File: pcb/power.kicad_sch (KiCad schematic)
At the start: 42 parts, among them Q1 AO3400A, U1 SIC431AED-T1-GE3, U2 TPS564247DRLR

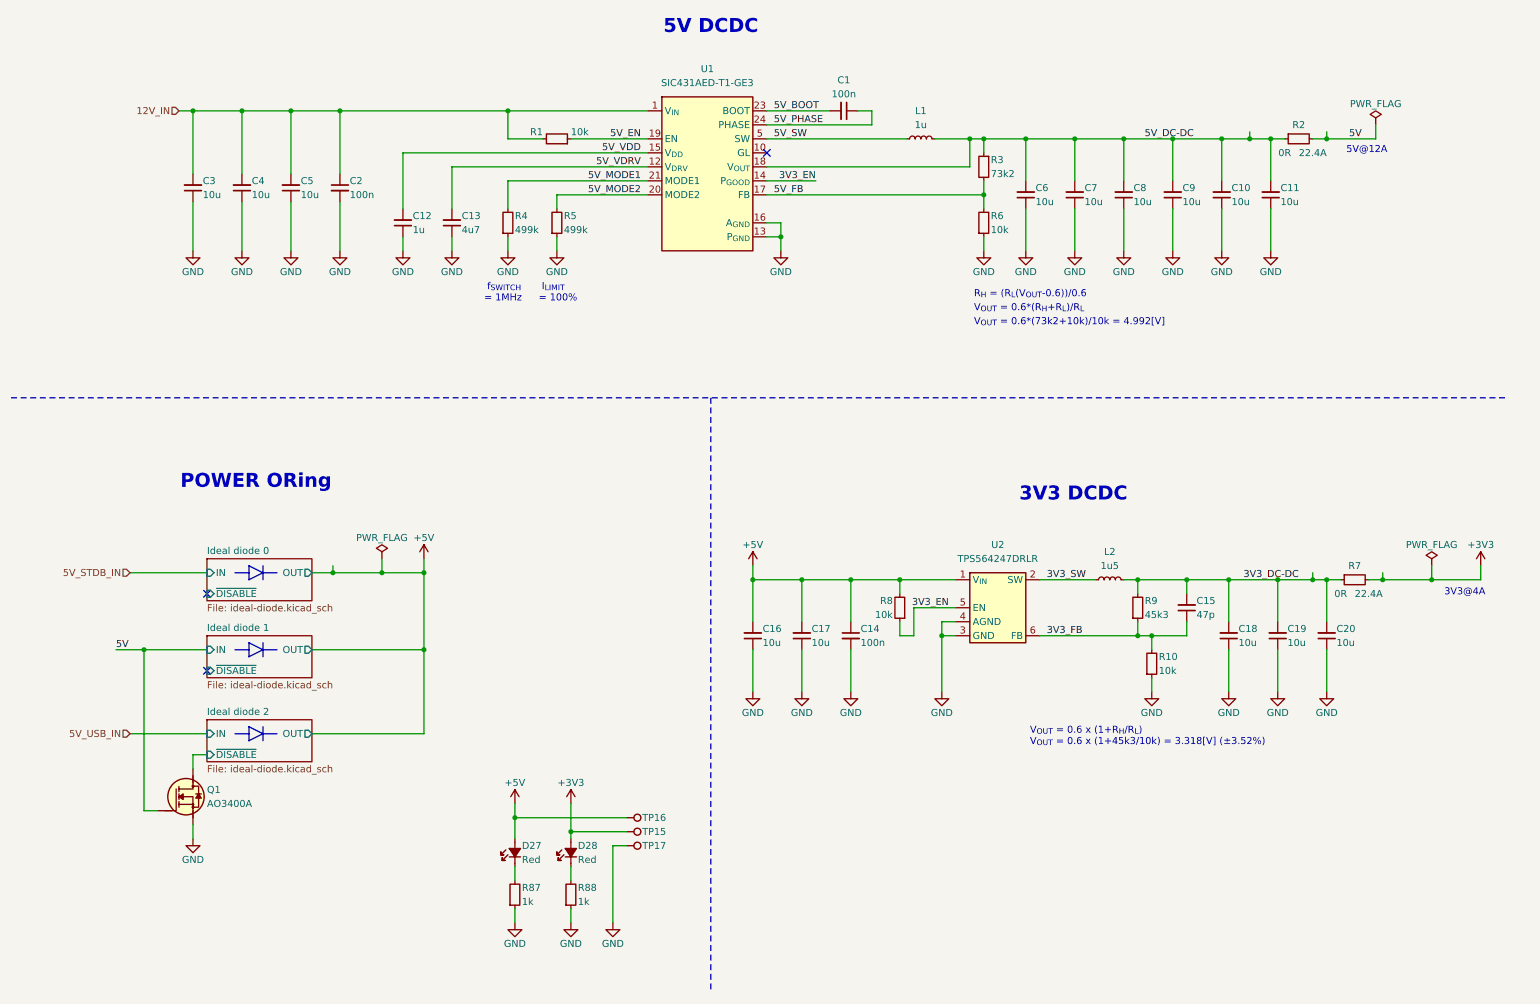
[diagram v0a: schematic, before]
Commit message: [#5] Refactor the schematic
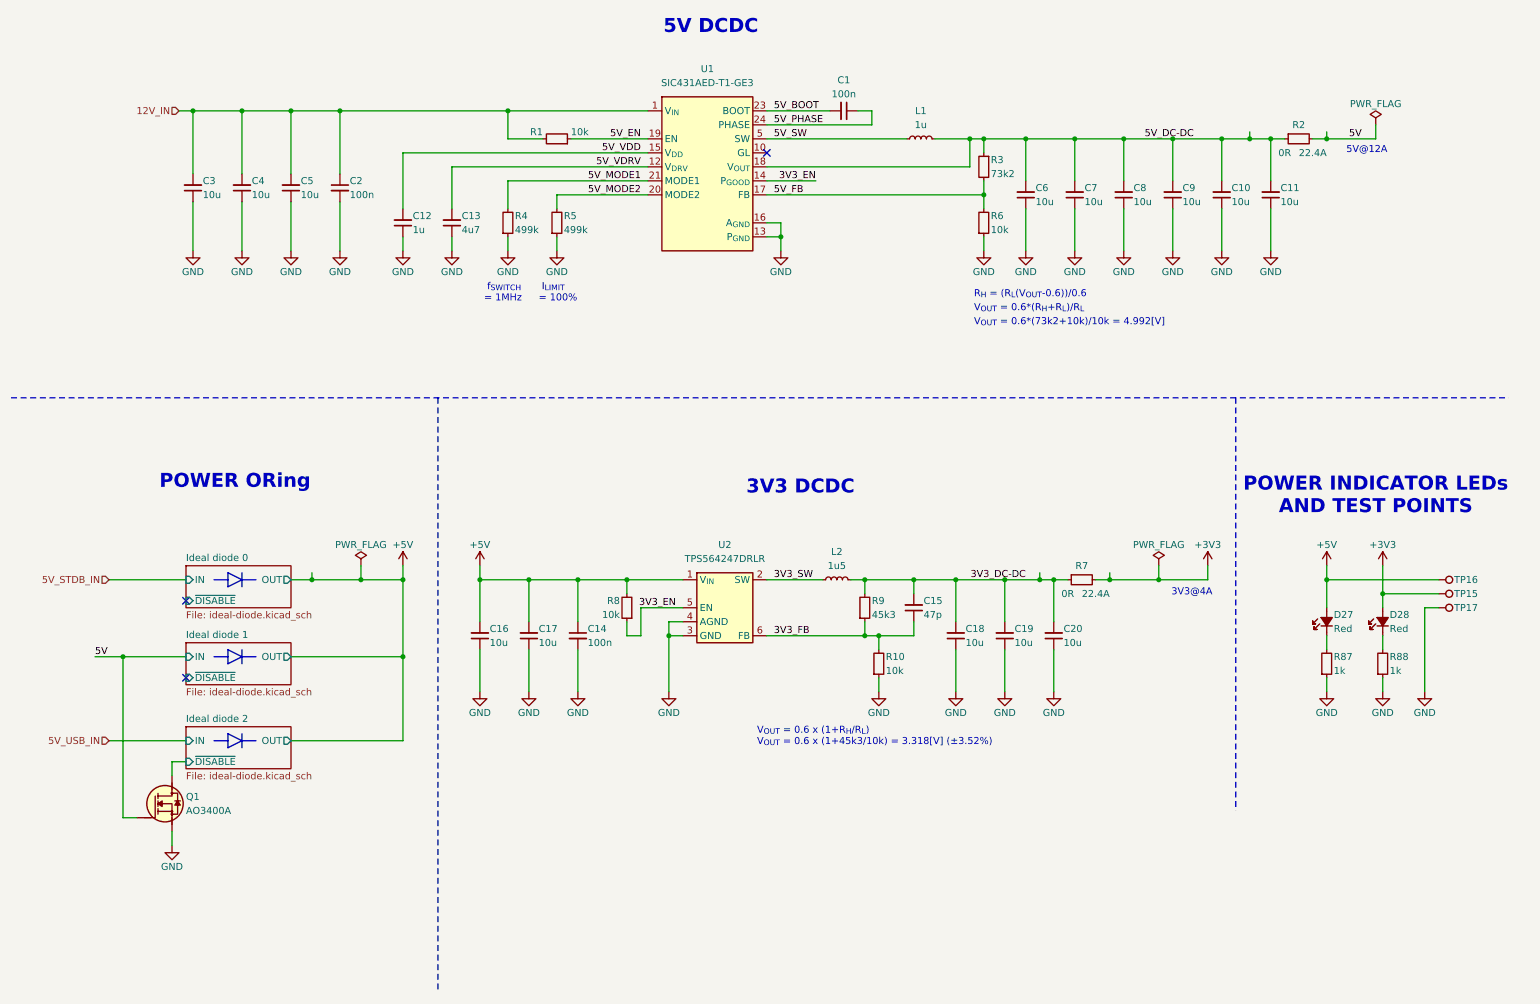
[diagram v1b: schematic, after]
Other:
- note added: "POWER INDICATOR LEDs AND TEST POINTS"
- moved on the sheet: C14, C15, C16, C17, C18, C19, C20, D27, D28, L2, Q1, R10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

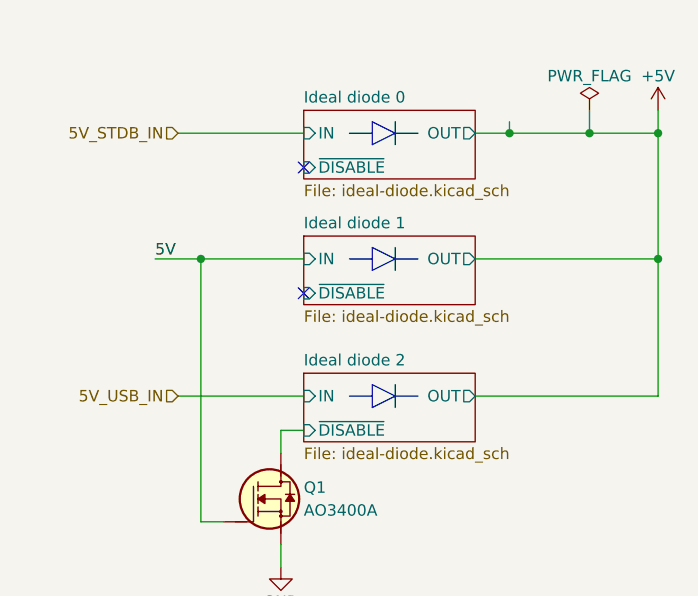
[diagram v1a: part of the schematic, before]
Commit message: [#5] Disable 5V_STDBY when main 5V rail is present
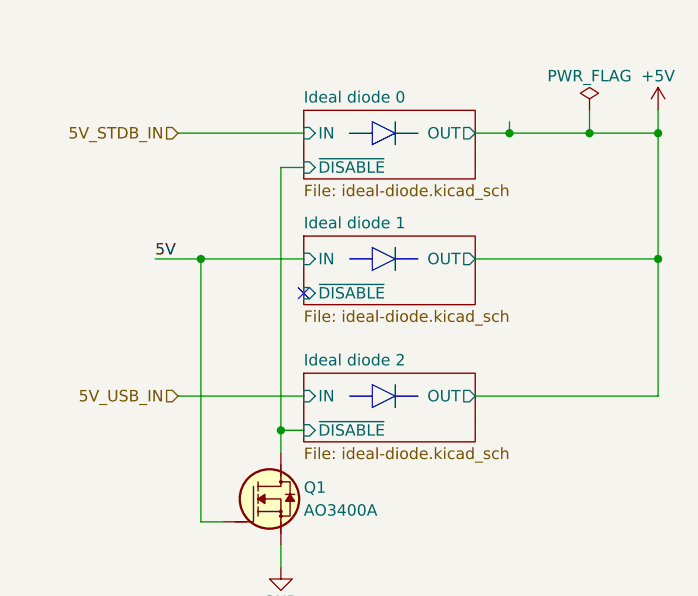
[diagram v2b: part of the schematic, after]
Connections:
- net Ideal diode 2/~{DISABLE} is gone; now on net Ideal diode 0/~{DISABLE}: Q1.3 (D)
- no-connect marks 3 -> 2
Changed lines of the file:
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@@
+	)
+	(junction
+		(at 41.91 156.21)
+		(diameter 0)
+		(color 0 0 0 0)
 	)
 	(junction
@@
 	)
 	(no_connect
-		(at 44.45 127)
-	)
-	(no_connect
 		(at 44.45 140.97)
 	)
@@
 	(wire
 		(pts
+			(xy 41.91 156.21) (xy 41.91 127)
+		)
+		(stroke
+			(width 0)
+			(type default)
+		)
+	)
+	(wire
+		(pts
 			(xy 167.64 130.81) (xy 167.64 133.35)
 		)
@@
 		)
 		(stroke
+			(width 0)
+			(type default)
+		)
+	)
+	(wire
+		(pts
+			(xy 41.91 127) (xy 44.45 127)
+		)
+		(stroke
